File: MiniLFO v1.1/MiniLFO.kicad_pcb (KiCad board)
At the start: 2 copper layers, 31.2 x 128.5 mm, 26 parts, among them J1 IDC_2x05, U1 TL074

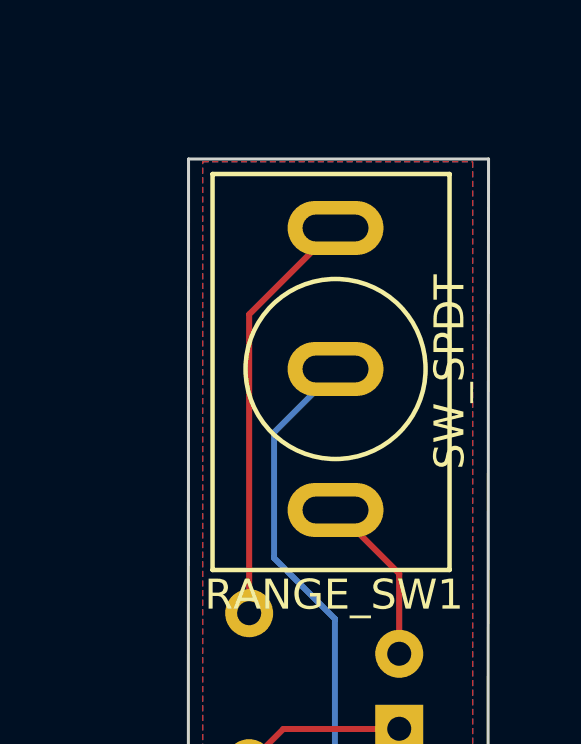
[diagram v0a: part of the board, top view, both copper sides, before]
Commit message: Updated BOM with parts numbers
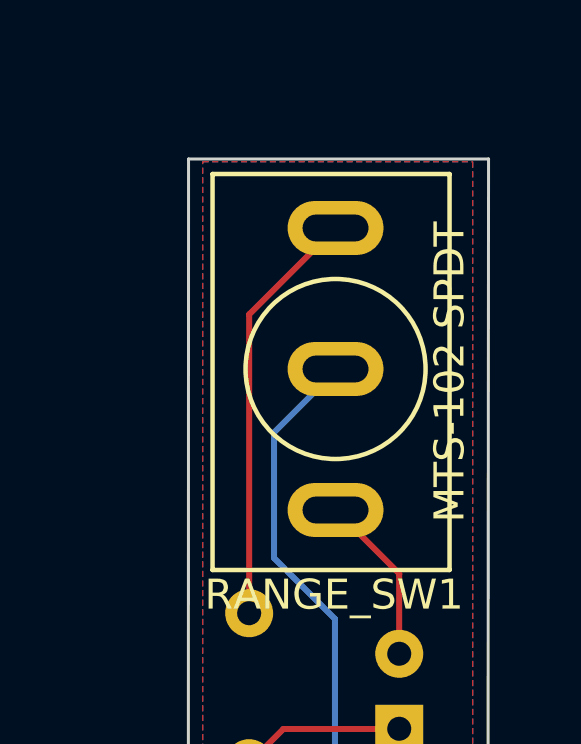
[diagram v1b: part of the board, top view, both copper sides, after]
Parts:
- RANGE_SW1: value SW_SPDT -> MTS-102 SPDT
- TRI_OUT1: value AudioJack2_SwitchT -> PJ-3001F
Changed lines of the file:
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@@
   (footprint "benjiaomodular:Potentiometer_RV09" (layer "F.Cu")
     (at 162.675 98.25 90)
+    (property "Manufacturers Name" "Alpha (Taiwan)")
+    (property "Manufacturers Part Number" "RV09AF-40-20K-B100K")
     (property "Sheetfile" "MiniLFO.kicad_sch")
     (property "Sheetname" "")
@@
   (footprint "benjiaomodular:Potentiometer_RV09" (layer "F.Cu")
     (at 162.625 118.45 90)
+    (property "Manufacturers Name" "Alpha (Taiwan)")
+    (property "Manufacturers Part Number" "RV09AF-40-20K-B100K")
     (property "Sheetfile" "MiniLFO.kicad_sch")
     (property "Sheetname" "")
@@
       (effects (font (size 1 1) (thickness 0.15)))
     )
-    (fp_text value "AudioJack2_SwitchT" (at 0 14) (layer "F.SilkS") hide
+    (fp_text value "PJ-3001F" (at 0 14) (layer "F.SilkS") hide
       (effects (font (size 1 1) (thickness 0.15)))
     )
@@
     (descr "Capacitor SMD 0603 (1608 Metric), square (rectangular) end terminal, IPC_7351 nominal with elongated pad for handsoldering. (Body size source: IPC-SM-782 page 76, https://www.pcb-3d.com/wordpress/wp-content/uploads/ipc-sm-782a_amendment_1_and_2.pdf), generated with kicad-footprint-generator")
     (tags "capacitor handsolder")
+    (property "Manufacturers Name" "KEMET")
+    (property "Manufacturers Part Number" "R82EC3100DQ70K ")
     (property "Sheetfile" "MiniLFO.kicad_sch")
     (property "Sheetname" "")
@@
     (descr "Capacitor SMD 0603 (1608 Metric), square (rectangular) end terminal, IPC_7351 nominal with elongated pad for handsoldering. (Body size source: IPC-SM-782 page 76, https://www.pcb-3d.com/wordpress/wp-content/uploads/ipc-sm-782a_amendment_1_and_2.pdf), generated with kicad-footprint-generator")
     (tags "capacitor handsolder")
+    (property "Manufacturers Name" "KEMET")
+    (property "Manufacturers Part Number" "R82EC3100DQ70K ")
     (property "Sheetfile" "MiniLFO.kicad_sch")
     (property "Sheetname" "")
@@
   (footprint "benjiaomodular:ToggleSwitch_MTS-102_SPDT" (layer "F.Cu")
     (at 165.15 71 180)
+    (property "Manufacturers Name" "Tayda Electronics")
+    (property "Manufacturers Part Number" "Mini Toggle Switch SPDT On-On")
     (property "Sheetfile" "MiniLFO.kicad_sch")
     (property "Sheetname" "")
@@
       (effects (font (size 1 1) (thickness 0.15)))
     )
-    (fp_text value "SW_SPDT" (at -3.8 -0.1 90) (layer "F.SilkS")
+    (fp_text value "MTS-102 SPDT" (at -3.8 -0.1 90) (layer "F.SilkS")
       (effects (font (size 1 1) (thickness 0.15)))
     )
@@
     (descr "LED, diameter 3.0mm, 2 pins")
     (tags "LED diameter 3.0mm 2 pins")
+    (property "Manufacturers Name" "KENTO")
+    (property "Manufacturers Part Number" "3ARG4HWC")
     (property "Sheetfile" "MiniLFO.kicad_sch")
     (property "Sheetname" "")
@@
   (footprint "benjiaomodular:Capacitor_Radial_D5.0mm_P2.5mm" (layer "B.Cu")
     (at 167.273 82.993113 90)
+    (property "Manufacturers Name" " Panasonic")
+    (property "Manufacturers Part Number" "ECE-A1VN100UB")
     (property "Sheetfile" "MiniLFO.kicad_sch")
     (property "Sheetname" "")
@@
     (descr "Resistor SMD 0603 (1608 Metric), square (rectangular) end terminal, IPC_7351 nominal with elongated pad for handsoldering. (Body size source: IPC-SM-782 page 72, https://www.pcb-3d.com/wordpress/wp-content/uploads/ipc-sm-782a_amendment_1_and_2.pdf), generated with kicad-footprint-generator")
     (tags "resistor handsolder")
+    (property "Manufacturers Name" "YAGEO")
+    (property "Manufacturers Part Number" "RC0603FR-07100KL ")
     (property "Sheetfile" "MiniLFO.kicad_sch")
     (property "Sheetname" "")
@@
     (descr "Resistor SMD 0603 (1608 Metric), square (rectangular) end terminal, IPC_7351 nominal with elongated pad for handsoldering. (Body size source: IPC-SM-782 page 72, https://www.pcb-3d.com/wordpress/wp-content/uploads/ipc-sm-782a_amendment_1_and_2.pdf), generated with kicad-footprint-generator")
     (tags "resistor handsolder")
+    (property "Manufacturers Name" "YAGEO")
+    (property "Manufacturers Part Number" "RC0603FR-07100KL ")
     (property "Sheetfile" "MiniLFO.kicad_sch")
     (property "Sheetname" "")
@@
     (descr "Resistor SMD 0603 (1608 Metric), square (rectangular) end terminal, IPC_7351 nominal with elongated pad for handsoldering. (Body size source: IPC-SM-782 page 72, https://www.pcb-3d.com/wordpress/wp-content/uploads/ipc-sm-782a_amendment_1_and_2.pdf), generated with kicad-footprint-generator")
     (tags "resistor handsolder")
+    (property "Manufacturers Name" "YAGEO")
+    (property "Manufacturers Part Number" "RC0603FR-07100KL ")
     (property "Sheetfile" "MiniLFO.kicad_sch")
     (property "Sheetname" "")
@@
     (descr "SOIC, 14 Pin (JEDEC MS-012AB, https://www.analog.com/media/en/package-pcb-resources/package/pkg_pdf/soic_narrow-r/r_14.pdf), generated with kicad-footprint-generator ipc_gullwing_generator.py")
     (tags "SOIC SO")
+    (property "Manufacturers Name" "STMicroelectronics")
+    (property "Manufacturers Part Number" "TL074ACDT")
     (property "Sheetfile" "MiniLFO.kicad_sch")
     (property "Sheetname" "")
@@
     (descr "Resistor SMD 0603 (1608 Metric), square (rectangular) end terminal, IPC_7351 nominal with elongated pad for handsoldering. (Body size source: IPC-SM-782 page 72, https://www.pcb-3d.com/wordpress/wp-content/uploads/ipc-sm-782a_amendment_1_and_2.pdf), generated with kicad-footprint-generator")
     (tags "resistor handsolder")
+    (property "Manufacturers Name" "YAGEO")
+    (property "Manufacturers Part Number" "AC0603FR-0710KL")
     (property "Sheetfile" "MiniLFO.kicad_sch")
     (property "Sheetname" "")
@@
     (descr "Resistor SMD 0603 (1608 Metric), square (rectangular) end terminal, IPC_7351 nominal with elongated pad for handsoldering. (Body size source: IPC-SM-782 page 72, https://www.pcb-3d.com/wordpress/wp-content/uploads/ipc-sm-782a_amendment_1_and_2.pdf), generated with kicad-footprint-generator")
     (tags "resistor handsolder")
+    (property "Manufacturers Name" "YAGEO")
+    (property "Manufacturers Part Number" "RC0603FR-074K7L")
     (property "Sheetfile" "MiniLFO.kicad_sch")
     (property "Sheetname" "")
@@
     (descr "Resistor SMD 0603 (1608 Metric), square (rectangular) end terminal, IPC_7351 nominal with elongated pad for handsoldering. (Body size source: IPC-SM-782 page 72, https://www.pcb-3d.com/wordpress/wp-content/uploads/ipc-sm-782a_amendment_1_and_2.pdf), generated with kicad-footprint-generator")
     (tags "resistor handsolder")
+    (property "Manufacturers Name" "YAGEO")
+    (property "Manufacturers Part Number" "RC0603FR-071KL ")
     (property "Sheetfile" "MiniLFO.kicad_sch")
     (property "Sheetname" "")
@@
   (footprint "benjiaomodular:Capacitor_Rect_L7.2mm_W2.5mm_P5.00mm" (layer "B.Cu")
     (at 162.27 84.14 90)
+    (property "Manufacturers Name" "KEMET")
+    (property "Manufacturers Part Number" "MMK5103K50J01L4BULK")
     (property "Sheetfile" "MiniLFO.kicad_sch")
     (property "Sheetname" "")
@@
     (descr "Resistor SMD 0603 (1608 Metric), square (rectangular) end terminal, IPC_7351 nominal with elongated pad for handsoldering. (Body size source: IPC-SM-782 page 72, https://www.pcb-3d.com/wordpress/wp-content/uploads/ipc-sm-782a_amendment_1_and_2.pdf), generated with kicad-footprint-generator")
     (tags "resistor handsolder")
+    (property "Manufacturers Name" "YAGEO")
+    (property "Manufacturers Part Number" "RC0603FR-7W470RL")
     (property "Sheetfile" "MiniLFO.kicad_sch")
     (property "Sheetname" "")
@@
     (descr "Resistor SMD 0603 (1608 Metric), square (rectangular) end terminal, IPC_7351 nominal with elongated pad for handsoldering. (Body size source: IPC-SM-782 page 72, https://www.pcb-3d.com/wordpress/wp-content/uploads/ipc-sm-782a_amendment_1_and_2.pdf), generated with kicad-footprint-generator")
     (tags "resistor handsolder")
-    (property "Sheetfile" "MiniLFO.kicad_sch")
-    (property "Sheetname" "")
+    (property "Manufacturers Name" "YAGEO")
+    (property "Manufacturers Part Number" "RC0603FR-071KL ")
+    (property "Sheetfile" "MiniLFO.kicad_sch")
+    (property "Sheetname" "")
